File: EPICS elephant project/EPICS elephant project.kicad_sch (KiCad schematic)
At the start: 1 part, among them U1 ESP32-C3-WROOM-02

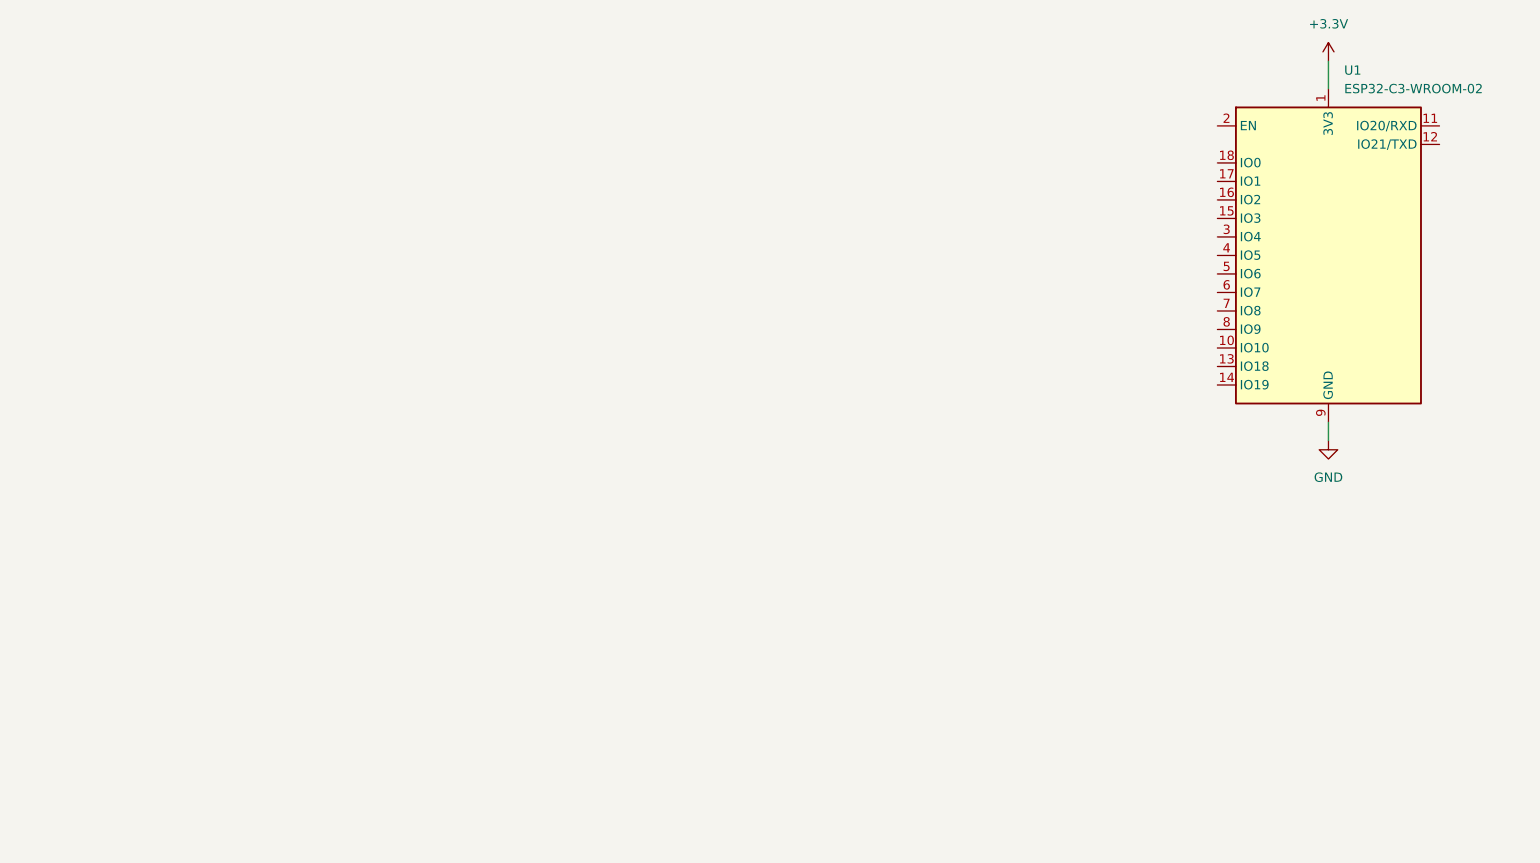
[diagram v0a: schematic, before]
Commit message: Adding the amplifiers for the circuit
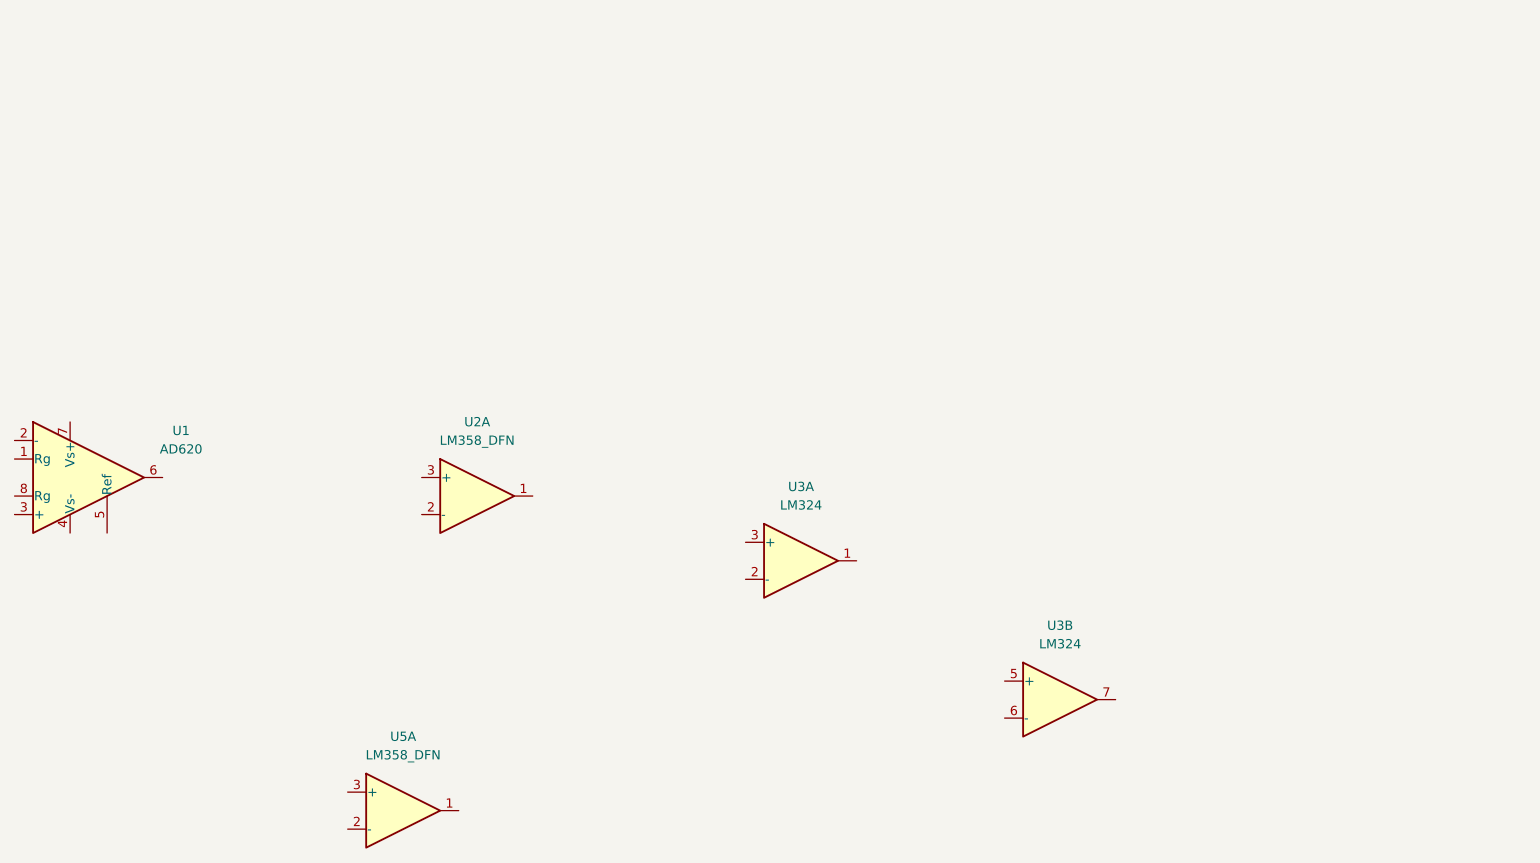
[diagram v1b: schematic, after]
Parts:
- removed U1: ESP32-C3-WROOM-02, RF_Module:ESP32-C3-WROOM-02, symbol RF_Module:ESP32-C3-WROOM-02
- added U1: AD620, symbol Amplifier_Instrumentation:AD620
- added U2, U5: LM358_DFN, Package_DFN_QFN:DFN-8-1EP_2x2mm_P0.5mm_EP1.05x1.75mm, symbol Amplifier_Operational:LM358_DFN
- added U3: LM324, symbol Amplifier_Operational:LM324

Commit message: Schematic wiring
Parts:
- added C1, C2: 1uF, symbol Device:C
- added R1, R10, R11, R2, R3, R4, R6, R8: 1k, symbol Device:R
- added R12: R, symbol Device:R
- added R5, R7: 10k, symbol Device:R
- added R9: 5.1k, symbol Device:R
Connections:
- net at U2.1: now also U2.2 (-), R2.1
- net at U2.3 (+): now also R1.2
- net at U5.1: now also U1.5 (Ref), U5.2 (-)
- net at U5.3 (+): now also R12.1, R4.1
- net at U3.1: now also U3.5 (+), C2.2, R9.2
- net at U3.2 (-): now also R5.2, R9.1
- net at U3.3 (+): now also C1.1, R3.2
- net at U3.6 (-): now also R7.1, R8.2
- net at U3.7: now also R7.2
- net at U1.2 (-): now also R10.2
- net at U1.3 (+): now also R11.2
- net at U1.6: now also R1.1
- new net: C2.1, R2.2, R3.1
- new net: R12.2, R6.2
- new net GND1: C1.2, R5.1, R8.1
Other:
- moved on the sheet: U5A

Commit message: Fixing simulation things
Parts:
- added V1: VSIN, symbol Simulation_SPICE:VSIN
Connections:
- net at R10.1: now also V1.1
- net at R11.1: now also V1.2
- net -VDC: now reaches U1.4 (Vs-)
- net +VDC: now reaches U1.7 (Vs+)
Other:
- moved on the sheet: C1, C2, R1, R10, R11, R12, R2, R3, R4, R5, R6, R7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

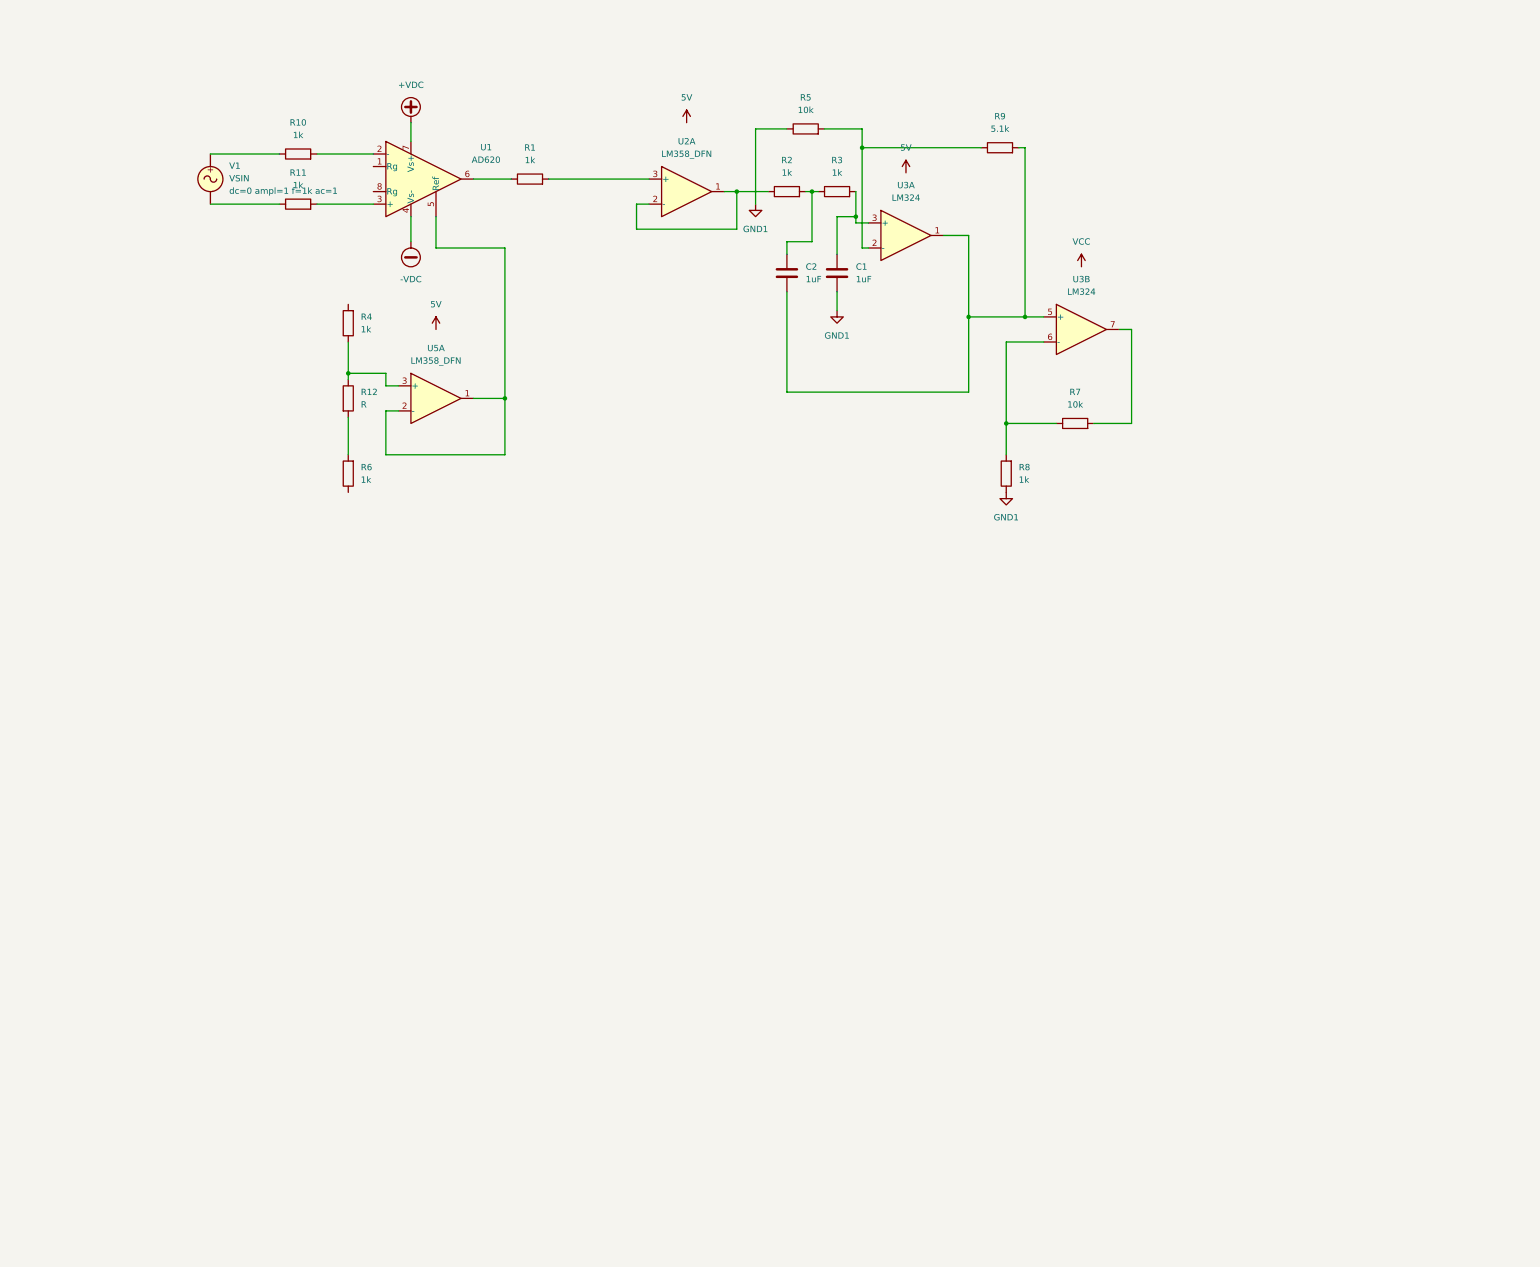
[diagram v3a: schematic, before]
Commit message: Added the exact components we need to use, also added an attenuation circuit step down from 5v to 3.3v for the ESP32 ADC read outs
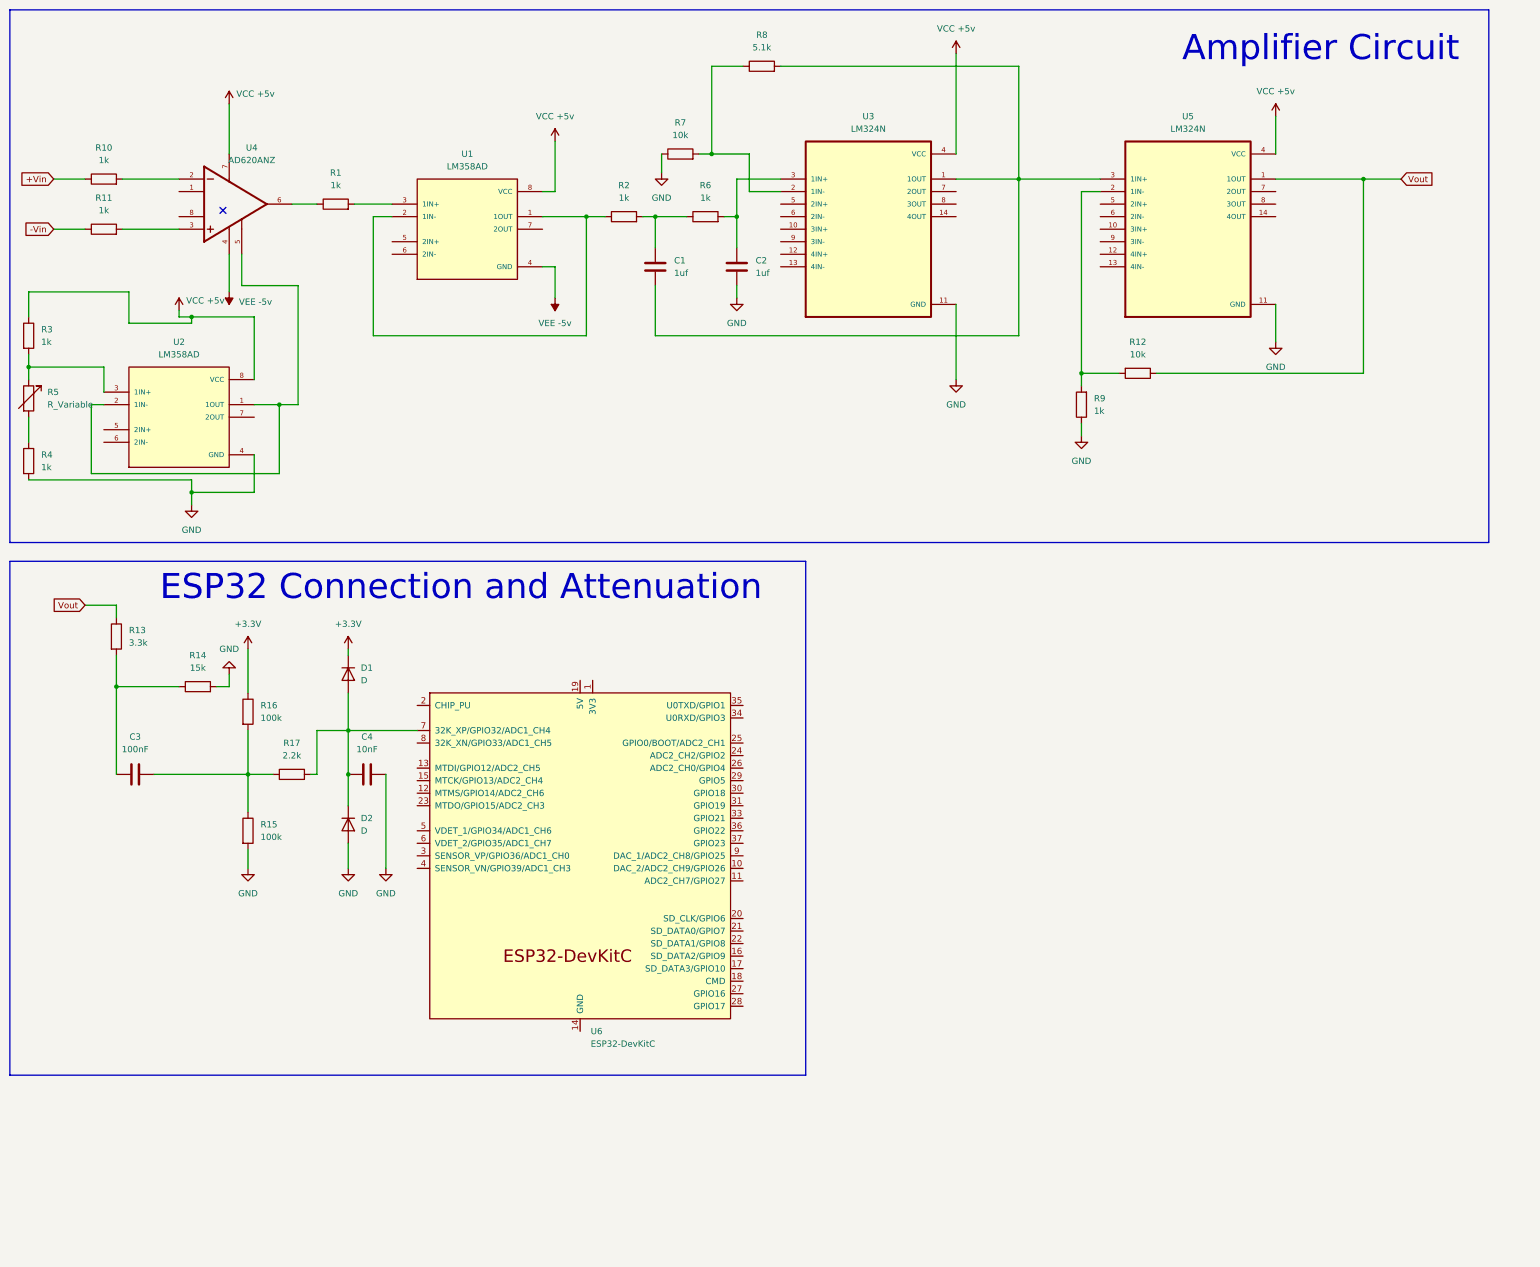
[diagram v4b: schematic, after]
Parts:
- removed R5: 10k, symbol Device:R
- removed U1: AD620, symbol Amplifier_Instrumentation:AD620
- removed U2, U5: LM358_DFN, Package_DFN_QFN:DFN-8-1EP_2x2mm_P0.5mm_EP1.05x1.75mm, symbol Amplifier_Operational:LM358_DFN
- removed U3: LM324, symbol Amplifier_Operational:LM324
- removed V1: VSIN, symbol Simulation_SPICE:VSIN
- added C3: 100nF, symbol Device:C
- added C4: 10nF, symbol Device:C
- added D1, D2: D, symbol Device:D
- added R13: 3.3k, symbol Device:R
- added R14: 15k, symbol Device:R
- added R15, R16: 100k, symbol Device:R
- added R17: 2.2k, symbol Device:R
- added R5: R_Variable, symbol Device:R_Variable
- added U1, U2: LM358AD, LM358AD:SOIC127P600X175-8N, symbol LM358AD:LM358AD
- added U3, U5: LM324N, LM324N:DIP794W45P254L1969H508Q14, symbol LM324N:LM324N
- added U4: AD620ANZ, AD620ANZ:DIP787W46P254L1016H533Q8, symbol AD620ANZ:AD620ANZ
- added U6: ESP32-DevKitC, PCM_Espressif:ESP32-DevKitC, symbol PCM_Espressif:ESP32-DevKitC
- C1, C2: value 1uF -> 1uf
- R12: value R -> 10k
- R8: value 1k -> 5.1k
- R9: value 5.1k -> 1k
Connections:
- net GND: now reaches R9.1
- net GND: now also C2.2, R4.2, R7.1, C4.1, D2.2 (A), R14.2, R15.2, U2.4 (GND), U3.11 (GND), U5.11 (GND)
- net at R2.1: now also U1.1 (1OUT), U1.2 (1IN-)
- net at R1.2: now also U1.3 (1IN+)
- net at C1.1: now also R2.2, R6.1; no longer R3.2
- net at R9.2: now also R12.2, U5.2 (1IN-); no longer C2.2
- net +Vin: now reaches R10.1
- net at R10.2: now also U4.2
- net at R4.1: now also R5.2; no longer R12.1
- net at R6.2: now also C2.1, U3.3 (1IN+); no longer R12.2
- net -Vin: now reaches R11.1
- net at R1.1: now also U4.6
- net at R8.2: now also C1.2, U3.1 (1OUT), U5.3 (1IN+); no longer R7.1
- net at R7.2: now also R8.1, U3.2 (1IN-)
- net at R11.2: now also U4.3
- removed net GND1: C1.2, R8.1
- new net: U6.14 (GND), U6.32 (GND), U6.38 (GND)
- new net: C4.2, D1.2 (A), D2.1 (K), R17.2, U6.7 (32K_XP/GPIO32/ADC1_CH4)
- new net: C3.1, R13.2, R14.1
- new net: C3.2, R15.1, R16.2, R17.1
- new net: U2.1 (1OUT), U2.2 (1IN-), U4.5
- new net: R3.2, R5.1, U2.3 (1IN+)
- new net +3.3V: D1.1 (K), R16.1
- new net VCC +5v: R3.1, U1.8 (VCC), U2.8 (VCC), U3.4 (VCC), U4.7, U5.4 (VCC)
- new net VEE -5v: U1.4 (GND), U4.4
- new net Vout: R12.1, R13.1, U5.1 (1OUT)
- no-connect marks 0 -> 1
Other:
- note added: "Amplifier Circuit"
- note added: "ESP32 Connection and Attenuation"
- moved on the sheet: R1, R10, R11

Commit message: Added decoupling circuit for ESP32
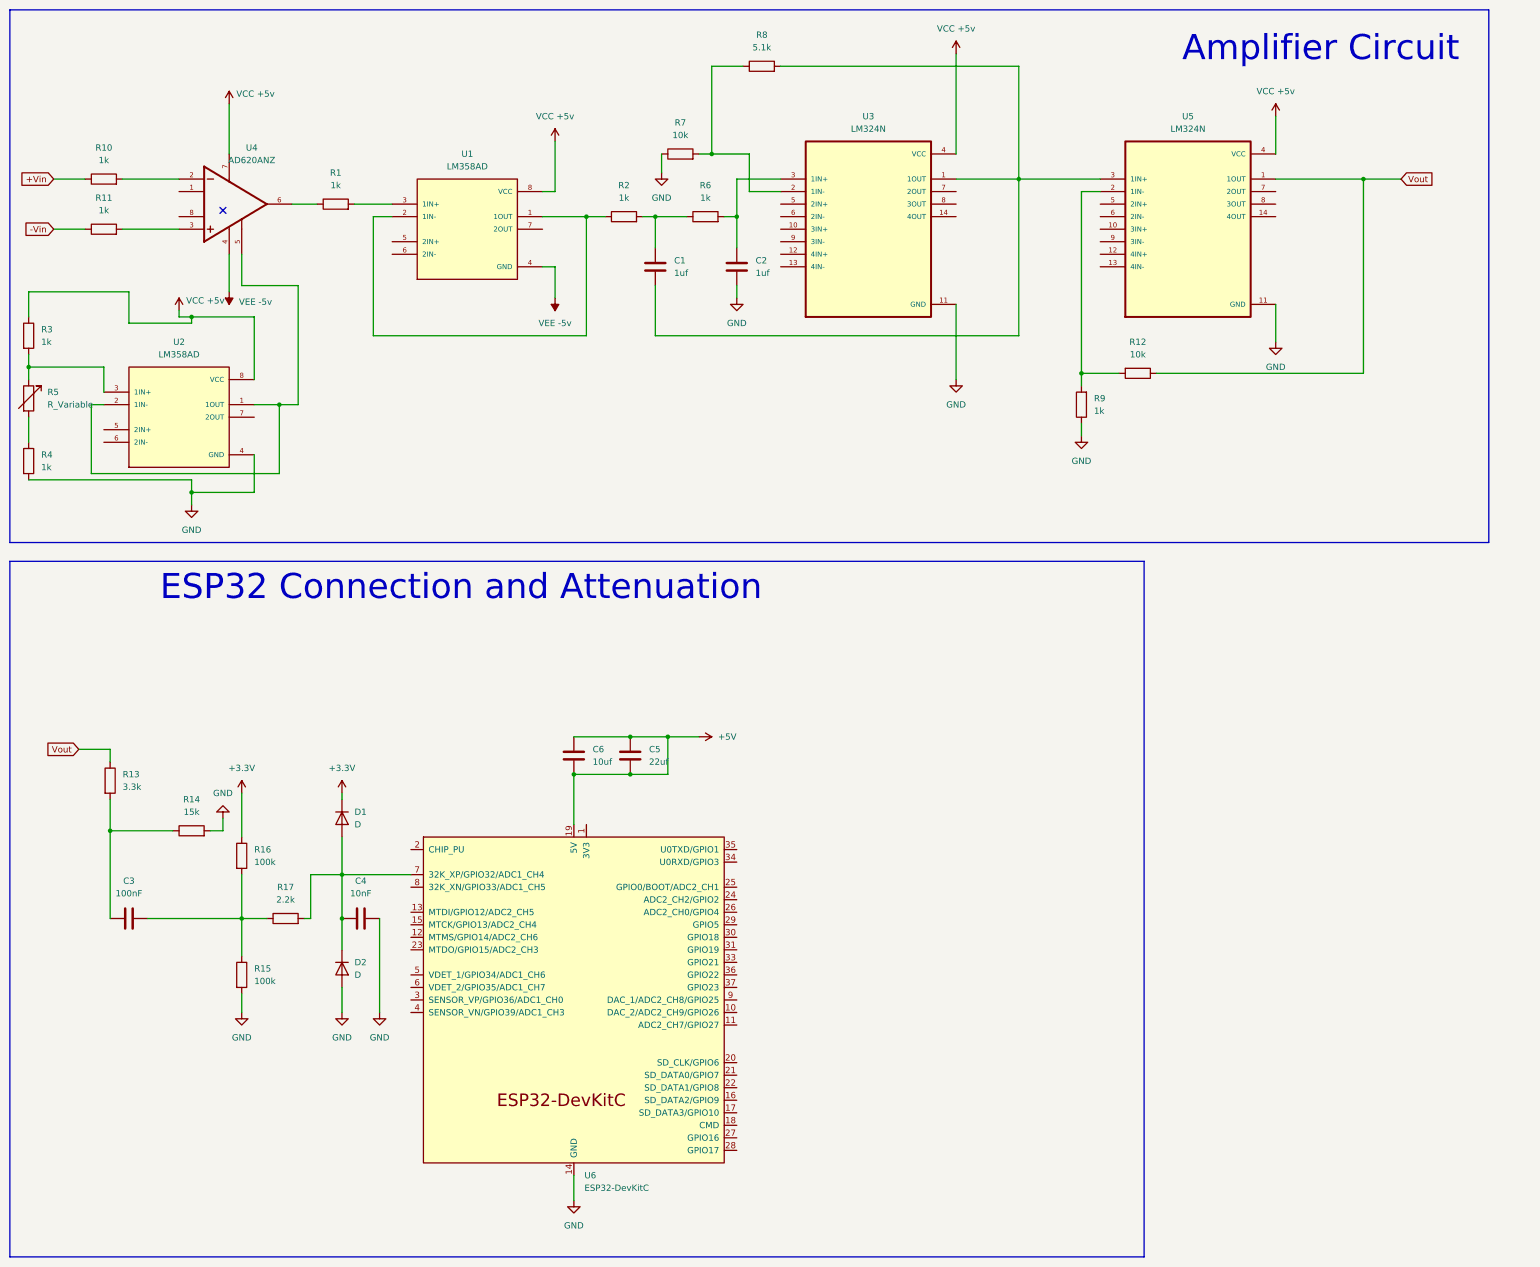
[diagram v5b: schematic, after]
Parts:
- added C5: 22uf, symbol Device:C
- added C6: 10uf, symbol Device:C
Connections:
- net GND: now also U6.14 (GND), U6.32 (GND), U6.38 (GND)
- net +5V: now reaches U6.19 (5V)
- net +5V: now also C5.1, C5.2, C6.1, C6.2
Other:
- moved on the sheet: C3, C4, D1, D2, R13, R14, R15, R16, R17, U6
